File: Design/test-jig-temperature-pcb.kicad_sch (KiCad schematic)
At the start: 44 parts, among them J1 Jack-DC, J10 Thermistor, J2 SWD, J3 Thermistor, J4 Thermistor, J5 Thermistor, J6 Thermistor, J7 Thermistor, J8 Thermistor, J9 Thermistor, Q1 BC547, U1 STM32G030C6Tx, U2 TL1117B-3.3

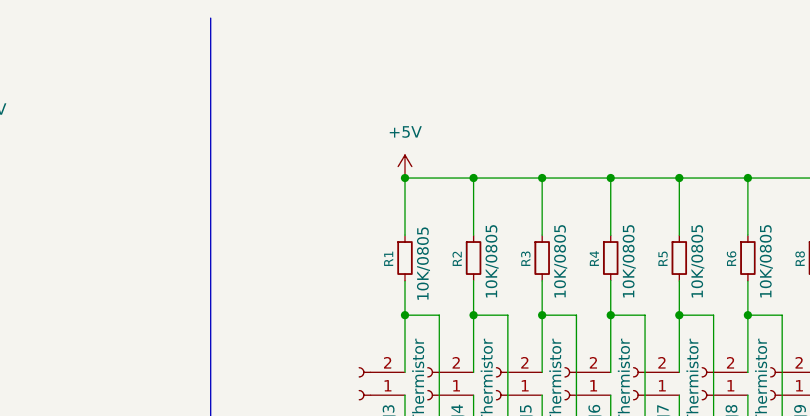
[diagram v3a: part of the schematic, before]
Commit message: Reposition thermistor connectors and re-route connections
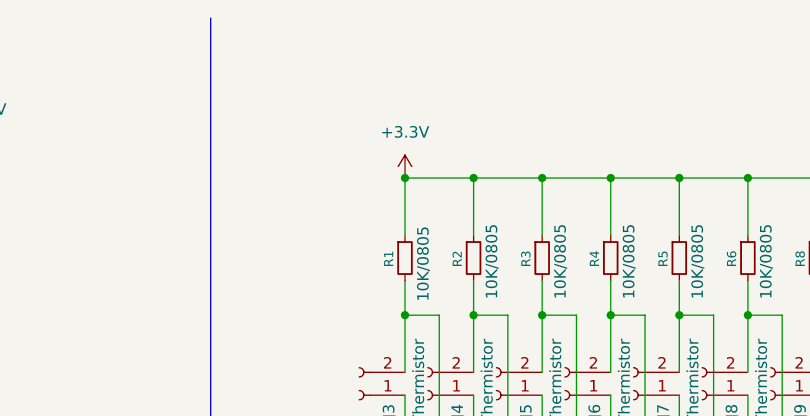
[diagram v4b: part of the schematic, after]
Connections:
- net +3.3V: now also R1.1, R10.1, R2.1, R3.1, R4.1, R5.1, R6.1, R8.1
- net +5V: no longer R1.1, R10.1, R2.1, R3.1, R4.1, R5.1, R6.1, R8.1
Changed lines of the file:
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@@
 	)
 	(junction
+		(at 212.09 30.48)
+		(diameter 0)
+		(color 0 0 0 0)
+	)
+	(junction
 		(at 119.38 33.02)
 		(diameter 0)
@@
 	)
 	(junction
-		(at 212.09 30.48)
-		(diameter 0)
-		(color 0 0 0 0)
-	)
-	(junction
 		(at 71.12 190.5)
 		(diameter 0)
@@
 	)
 	(symbol
+		(lib_id "power:+3.3V")
+		(at 212.09 30.48 0)
+		(unit 1)
+		(exclude_from_sim no)
+		(in_bom yes)
+		(on_board yes)
+		(dnp no)
+		(fields_autoplaced yes)
+		(property "Reference" "#PWR09"
+			(at 212.09 34.29 0)
+			(effects
+				(font
+					(size 1.27 1.27)
+				)
+				(hide yes)
+			)
+		)
+		(property "Value" "+3.3V"
+			(at 212.09 25.4 0)
+			(effects
+				(font
+					(size 1.27 1.27)
+				)
+			)
+		)
+		(property "Footprint" ""
+			(at 212.09 30.48 0)
+			(effects
+				(font
+					(size 1.27 1.27)
+				)
+				(hide yes)
+			)
+		)
+		(property "Datasheet" ""
+			(at 212.09 30.48 0)
+			(effects
+				(font
+					(size 1.27 1.27)
+				)
+				(hide yes)
+			)
+		)
+		(property "Description" "Power symbol creates a global label with name \"+3.3V\""
+			(at 212.09 30.48 0)
+			(effects
+				(font
+					(size 1.27 1.27)
+				)
+				(hide yes)
+			)
+		)
+		(pin "1"
+		)
+		(instances
+			(project "test-jig-temperature-pcb"
+				(path "/ee90df8d-0f55-4797-b97b-555aec38ead9"
+					(reference "#PWR09")
+					(unit 1)
+				)
+			)
+		)
+	)
+	(symbol
 		(lib_id "Display_Character:WC1602A")
 		(at 232.41 127 0)
@@
 					(unit 1)
 				)
-			)
-		)
-	)
-	(symbol
-		(lib_id "power:+5V")
-		(at 212.09 30.48 0)
-		(unit 1)
-		(exclude_from_sim no)
-		(in_bom yes)
-		(on_board yes)
-		(dnp no)
-		(fields_autoplaced yes)
-		(property "Reference" "#PWR015"
-			(at 212.09 34.29 0)
-			(effects
-				(font
-					(size 1.27 1.27)
-				)
-				(hide yes)
-			)
-		)
-		(property "Value" "+5V"
-			(at 212.09 25.4 0)
-			(effects
-				(font
-					(size 1.27 1.27)
-				)
-			)
-		)
-		(property "Footprint" ""
-			(at 212.09 30.48 0)
-			(effects
-				(font
-					(size 1.27 1.27)
-				)
-				(hide yes)
-			)
-		)
-		(property "Datasheet" ""
-			(at 212.09 30.48 0)
-			(effects
-				(font
-					(size 1.27 1.27)
-				)
-				(hide yes)
-			)
-		)
-		(property "Description" "Power symbol creates a global label with name \"+5V\""
-			(at 212.09 30.48 0)
-			(effects
-				(font
-					(size 1.27 1.27)
-				)
-				(hide yes)
-			)
-		)
-		(pin "1"
-		)
-		(instances
-			(project ""
-				(path "/ee90df8d-0f55-4797-b97b-555aec38ead9"
-					(reference "#PWR015")
-					(unit 1)
-				)
